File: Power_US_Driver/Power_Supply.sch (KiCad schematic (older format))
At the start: 6 parts, among them T1 Transformer_1P_1S, U1 LM7805_TO220

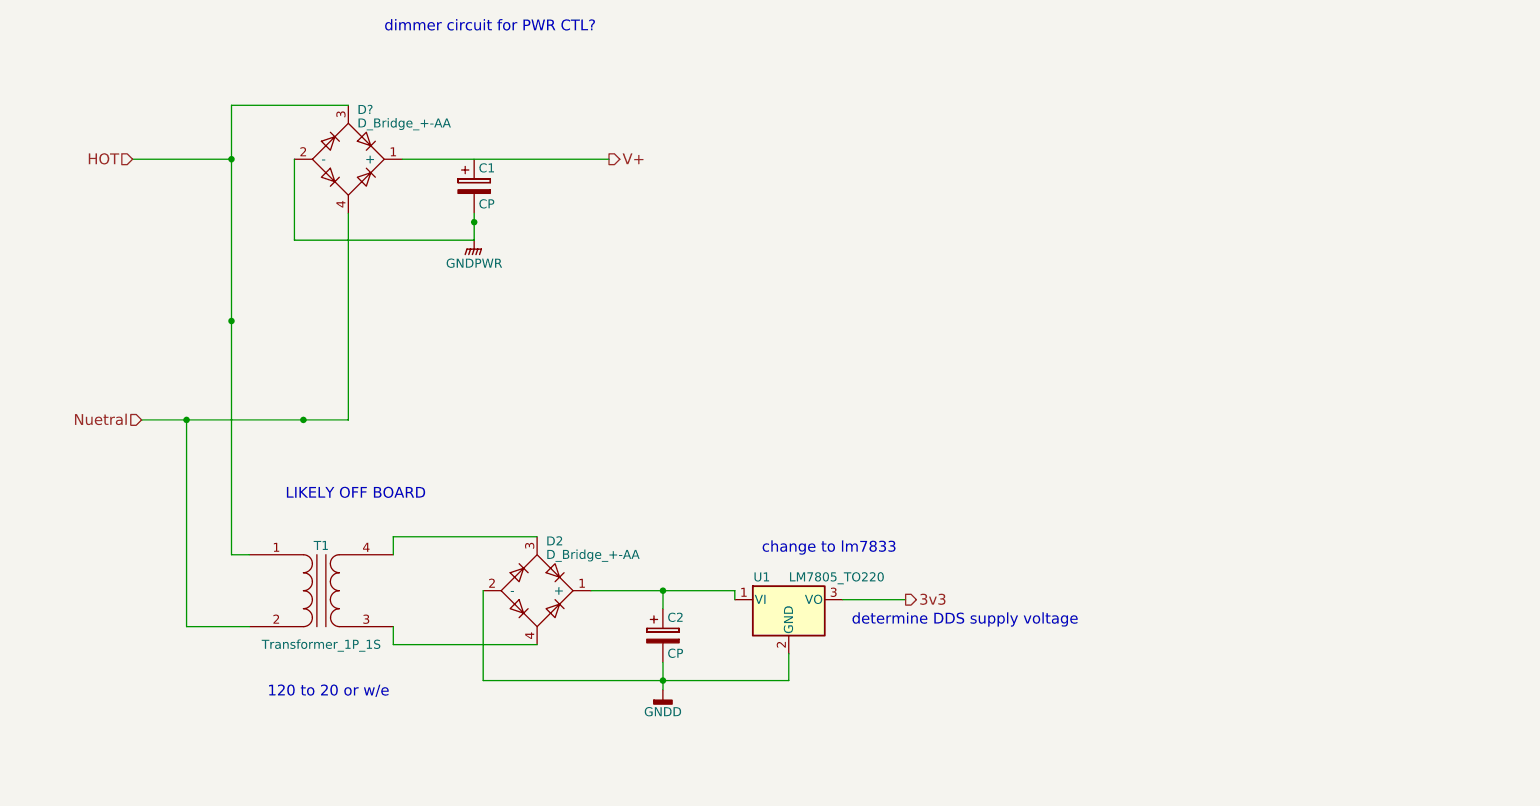
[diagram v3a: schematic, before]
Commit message: moved high current diode off board
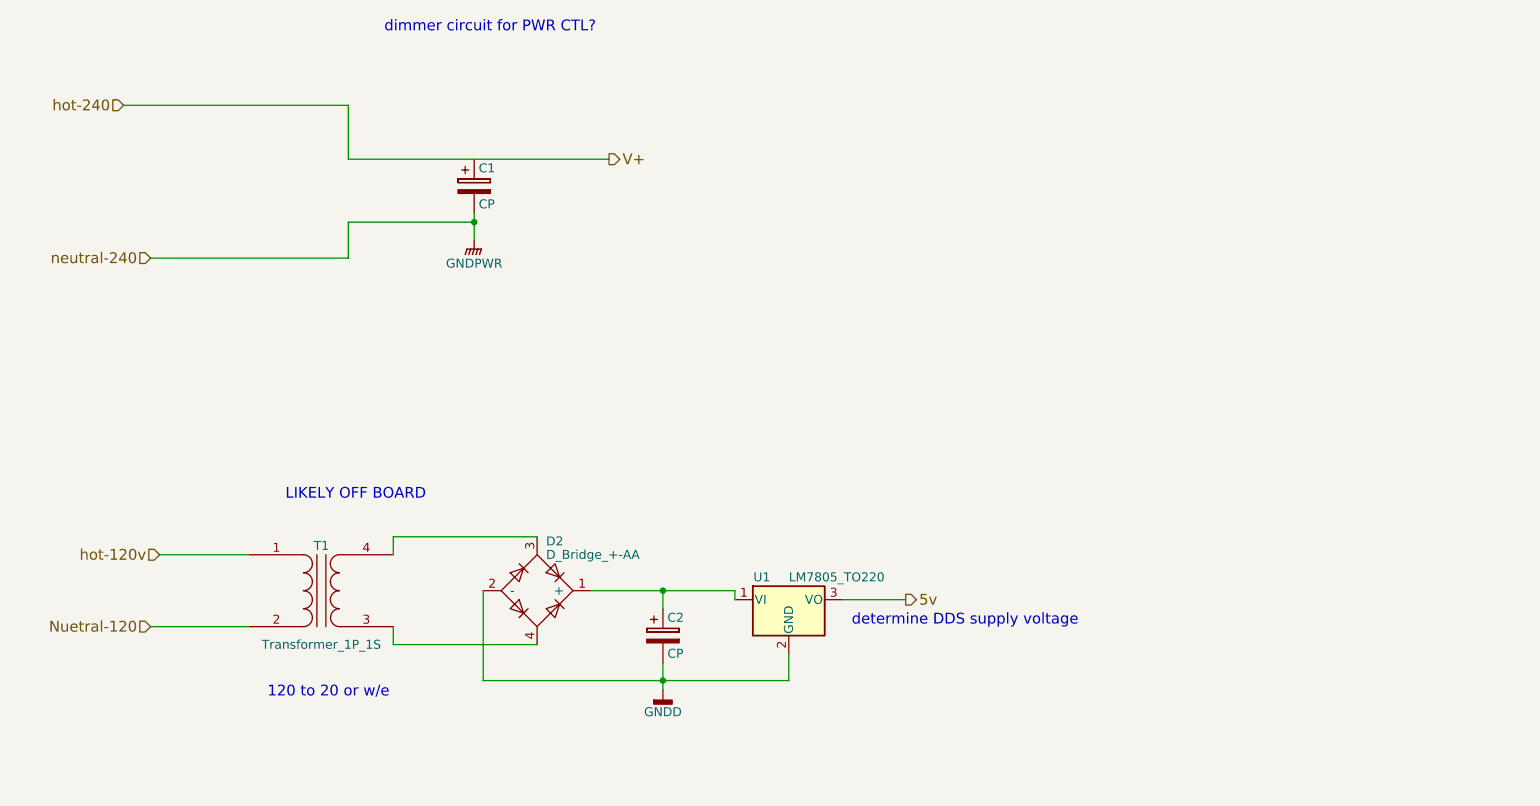
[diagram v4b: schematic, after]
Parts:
- removed D?: D_Bridge_+-AA, symbol D_Bridge_+-AA
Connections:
- net 3v3 renamed 5v
- net HOT renamed hot-120v
- net Nuetral renamed Nuetral-120
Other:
- note removed: "change to lm7833"
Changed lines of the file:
@@
 Text HLabel 3700 2000 2    60   Output ~ 0
 V+
-Text HLabel 1050 2000 0    60   Input ~ 0
-HOT
-Text HLabel 1100 3450 0    60   Input ~ 0
-Nuetral
+Text HLabel 1200 4200 0    60   Input ~ 0
+hot-120v
+Text HLabel 1150 4600 0    60   Input ~ 0
+Nuetral-120
 Text HLabel 5350 4450 2    60   Output ~ 0
-3v3
+5v
 $Comp
 L LM7805_TO220 U1
@@
 determine DDS supply voltage
 Wire Wire Line
-	1600 4200 1700 4200
+	1200 4200 1700 4200
 Wire Wire Line
-	1600 1700 1600 4200
-Connection ~ 1600 2000
-Wire Wire Line
-	1700 4600 1350 4600
-Wire Wire Line
-	1350 4600 1350 3450
-Connection ~ 1350 3450
+	1150 4600 1700 4600
 Wire Wire Line
 	2500 4200 2500 4100
@@
 Connection ~ 4000 4900
 $Comp
-L GNDPWR #PWR4
+L GNDPWR #PWR04
 U 1 1 5AB00CEA
 P 2950 2450
-F 0 "#PWR4" H 2950 2250 50  0001 C CNN
+F 0 "#PWR04" H 2950 2250 50  0001 C CNN
 F 1 "GNDPWR" H 2950 2320 50  0000 C CNN
 F 2 "" H 2950 2400 50  0001 C CNN
@@
 $EndComp
 $Comp
-L GNDD #PWR5
+L GNDD #PWR05
 U 1 1 5AB013C1
 P 4000 4950
-F 0 "#PWR5" H 4000 4700 50  0001 C CNN
+F 0 "#PWR05" H 4000 4700 50  0001 C CNN
 F 1 "GNDD" H 4000 4825 50  0000 C CNN
 F 2 "" H 4000 4950 50  0001 C CNN
@@
 Wire Wire Line
 	5350 4450 5000 4450
-Text Notes 4550 4200 0    60   ~ 0
-change to lm7833
 Wire Wire Line
-	3700 2000 2550 2000
+	2250 2000 3700 2000
 Wire Wire Line
 	2950 2300 2950 2450
 Connection ~ 2950 2350
-Connection ~ 2000 3450
-Wire Wire Line
-	1100 3450 2250 3450
-Connection ~ 1600 2900
 Text Notes 2450 1300 0    60   ~ 0
 dimmer circuit for PWR CTL?
-$Comp
-L D_Bridge_+-AA D?
-U 1 1 5AB2B456
-P 2250 2000
-F 0 "D?" H 2300 2275 50  0000 L CNN
-F 1 "D_Bridge_+-AA" H 2300 2200 50  0000 L CNN
-F 2 "" H 2250 2000 50  0001 C CNN
-F 3 "" H 2250 2000 50  0001 C CNN
-	1    2250 2000
-	1    0    0    -1
-$EndComp
 Wire Wire Line
-	1950 2000 1950 2450
+	1000 1700 2250 1700
+Text HLabel 1000 1700 0    60   Input ~ 0
+hot-240
+Text HLabel 1150 2550 0    60   Input ~ 0
+neutral-240
 Wire Wire Line
-	1950 2450 2950 2450
+	1150 2550 2250 2550
 Wire Wire Line
-	2250 3450 2250 2300
+	2250 2550 2250 2350
 Wire Wire Line
-	2250 1700 1600 1700
+	2250 2350 2950 2350
 Wire Wire Line
-	1050 2000 1600 2000
+	2250 1700 2250 2000
 $EndSCHEMATC
